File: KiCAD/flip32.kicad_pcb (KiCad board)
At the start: 2 copper layers, 36 x 36 mm, 57 parts, among them CON1 USB, IC2 MIC5205, Q1 MMBT29, U1 LP38691, U2 MPU-9150, U3 STM32F103CB, U5 MS5611-01BA, U6 CP2102, X1 8MHZ

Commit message: fixed some missing labels
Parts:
- added G***: LOGO, temp:bear-paw-med, B.Cu at (144.1, 151.3)
- renumbered JP2 to FSYNC-MPU
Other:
- board text added: "Twist32+"
- board text added: "by S.Antonio"
- board text added: "by S.Antonio 2015"
- board text added: "https://github.com/simonantonio/flip32plus/tree/mpu9150"
- board text added: "rev 20150717"

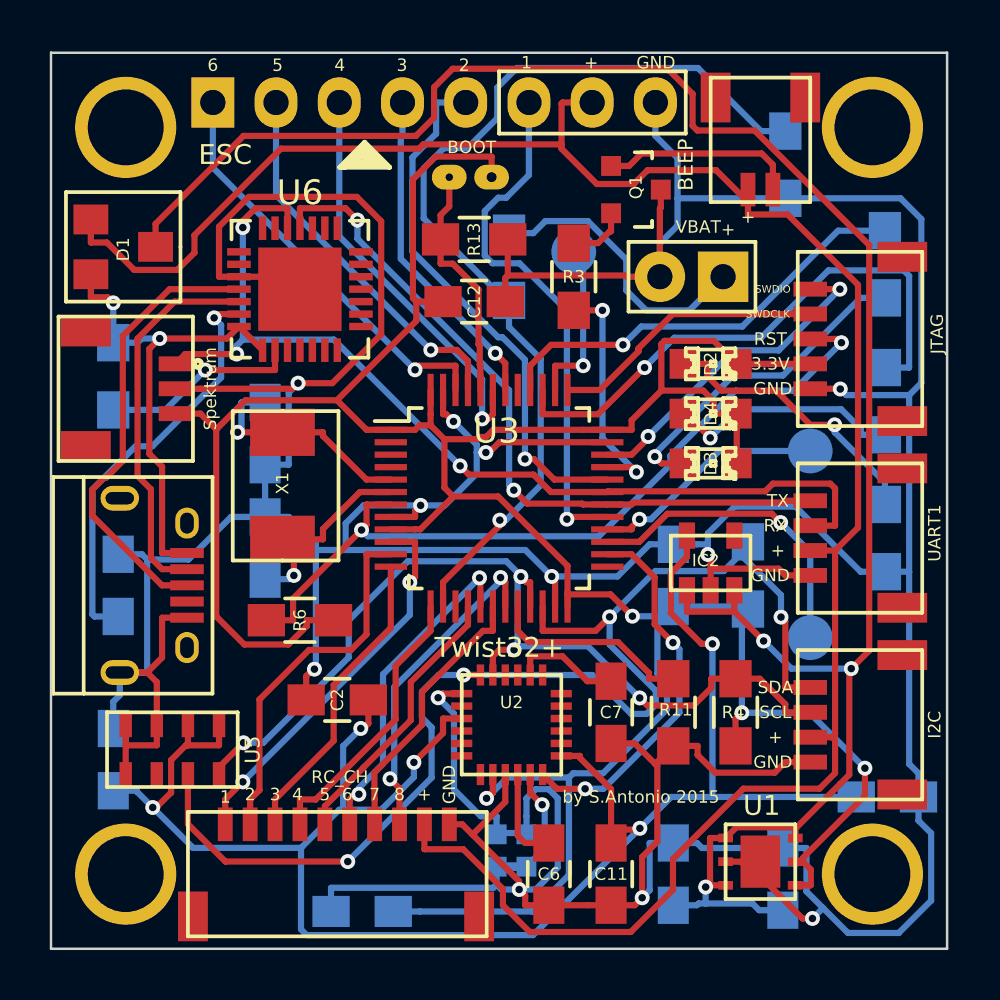
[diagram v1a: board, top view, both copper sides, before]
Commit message: swapped from old mpu9150 to newer mpu9250
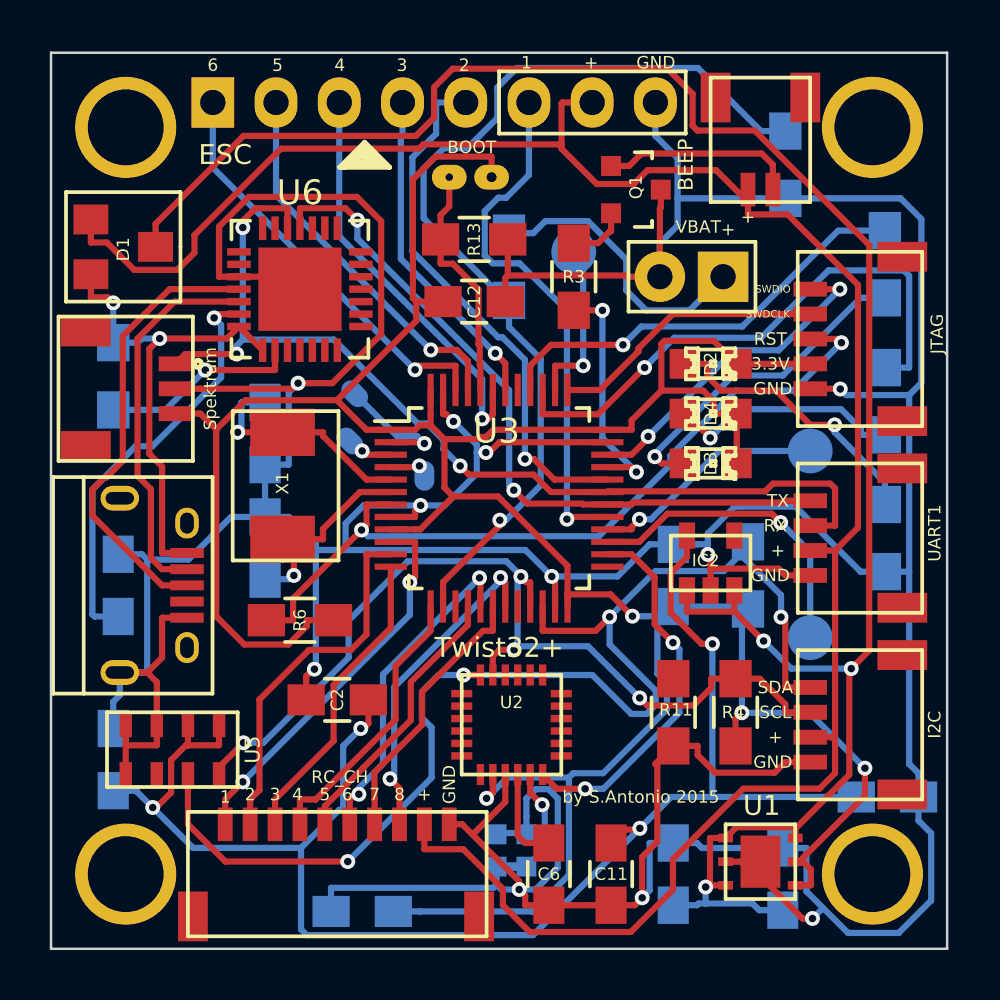
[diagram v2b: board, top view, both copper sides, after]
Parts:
- removed C7: 2.2nF 50v, Capacitors_SMD:C_0805_HandSoldering
- added PC13: UU5, Connect:1pin, B.Cu at (140.2, 141.7)
- added PC14: UU5, Connect:1pin, B.Cu at (140.0, 143.6)
- added PC15: UU5, Connect:1pin, B.Cu at (143.0, 145.0)
- U2: value MPU-9150 -> MPU-9250
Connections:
- U2 pad 1: N-0000024 -> (no net)
- U2 pad 18: N-0000071 -> GND
- U2 pad 20: N-0000032 -> GND
- U2 pad 22: N-0000052 -> VCC
- U2 pad 3: /VCC_SEN -> (no net)
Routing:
- net /VCC_SEN: track 74.5 -> 63.3 mm, vias 5 -> 4
- net /BOOT1: track 8.16 -> 0.00 mm
- net N-0000024: track 7.85 -> 0.00 mm, vias 1 -> 0
- net /UU3: track 0.00 -> 5.00 mm, vias 0 -> 1
- net N-0000032: track 4.41 -> 0.00 mm
- net GND: track 248.8 -> 246.7 mm
- net /UU4: track 0.00 -> 1.88 mm, vias 0 -> 1
- net /UU5: track 0.00 -> 1.65 mm, vias 0 -> 1

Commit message: redoing layout of traces for updated pinout of mpu9250
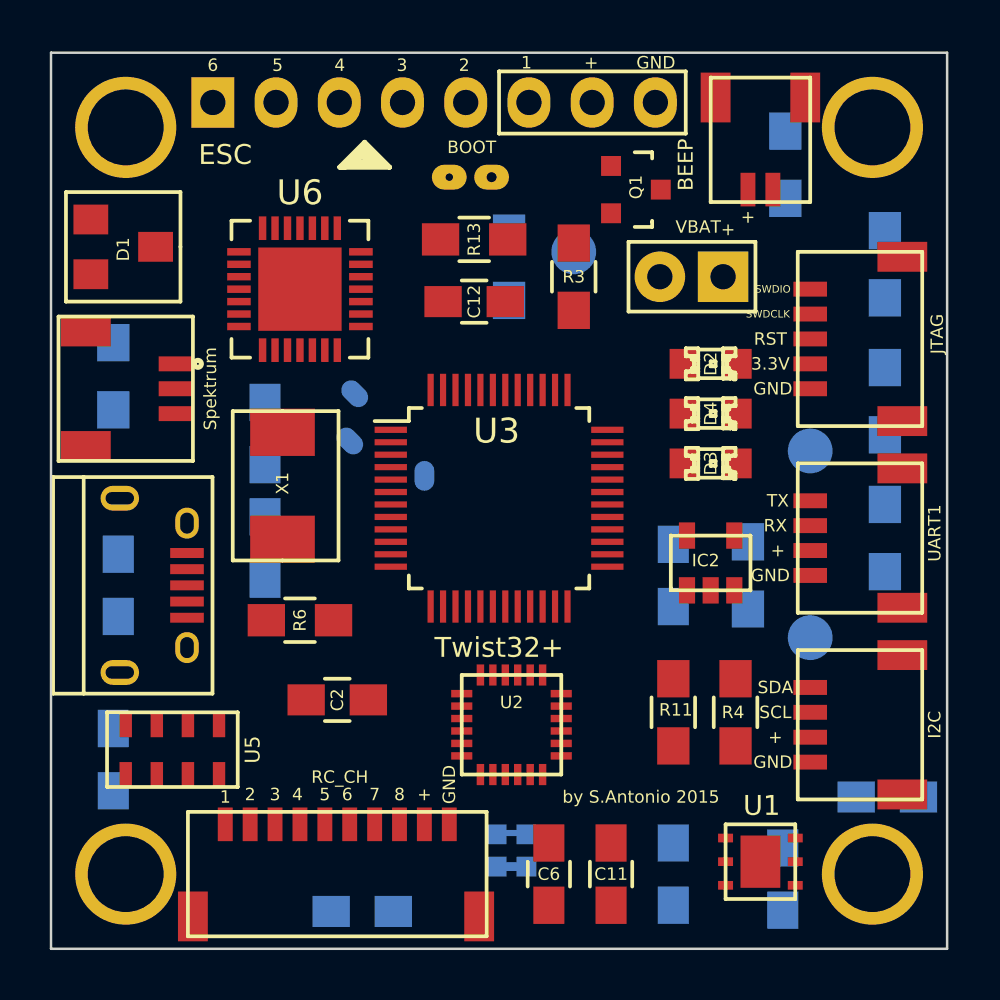
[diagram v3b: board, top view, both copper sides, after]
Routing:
- net GND: track 246.7 -> 0.00 mm, vias 11 -> 0
- net VCC: track 130.7 -> 0.00 mm, vias 4 -> 0
- net /VCC_IN: track 85.9 -> 0.00 mm
- net /TO_REGS: track 82.4 -> 0.00 mm, vias 3 -> 0
- net /VCC_SEN: track 63.3 -> 0.00 mm, vias 4 -> 0
- net /SDA: track 50.8 -> 0.00 mm, vias 4 -> 0
- net /RX0: track 40.1 -> 0.00 mm, vias 3 -> 0
- net /POWER_ADC: track 39.4 -> 0.00 mm, vias 1 -> 0
- net /SCL: track 37.4 -> 0.00 mm, vias 4 -> 0
- net /NRST: track 32.1 -> 0.00 mm, vias 2 -> 0
- net /TX0: track 29.0 -> 0.00 mm, vias 2 -> 0
- net /LED1: track 22.8 -> 0.00 mm, vias 1 -> 0
- net /PWM2: track 21.5 -> 0.00 mm, vias 1 -> 0
- net /PWM1: track 21.3 -> 0.00 mm, vias 1 -> 0
- net /VBUS: track 20.2 -> 0.00 mm, vias 2 -> 0
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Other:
- board text added: "https://github.com/simonantonio/flip32plus/tree/mpu9250"
- board text added: "rev 20150720"
- board text removed: "https://github.com/simonantonio/flip32plus/tree/mpu9150"
- board text removed: "rev 20150717"

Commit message: pcb completed
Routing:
- net GND: track 0.00 -> 250.2 mm, vias 0 -> 5
- net VCC: track 0.00 -> 163.9 mm, vias 0 -> 7
- net /VCC_IN: track 0.00 -> 124.0 mm, vias 0 -> 3
- net /VCC_SEN: track 0.00 -> 78.0 mm, vias 0 -> 3
- net /TO_REGS: track 0.00 -> 72.5 mm, vias 0 -> 4
- net /SDA: track 0.00 -> 57.7 mm, vias 0 -> 4
- net /TX0: track 0.00 -> 48.0 mm, vias 0 -> 4
- net /RX0: track 0.00 -> 46.0 mm, vias 0 -> 5
- net /NRST: track 0.00 -> 38.6 mm, vias 0 -> 2
- net /SCL: track 0.00 -> 36.3 mm, vias 0 -> 3
- net /LED0: track 0.00 -> 35.2 mm, vias 0 -> 1
- net /PWM2: track 0.00 -> 32.0 mm, vias 0 -> 2
- net /POWER_ADC: track 0.00 -> 31.9 mm, vias 0 -> 1
- net /PWM1: track 0.00 -> 31.6 mm, vias 0 -> 1
- net /UU8: track 0.00 -> 30.2 mm, vias 0 -> 1
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
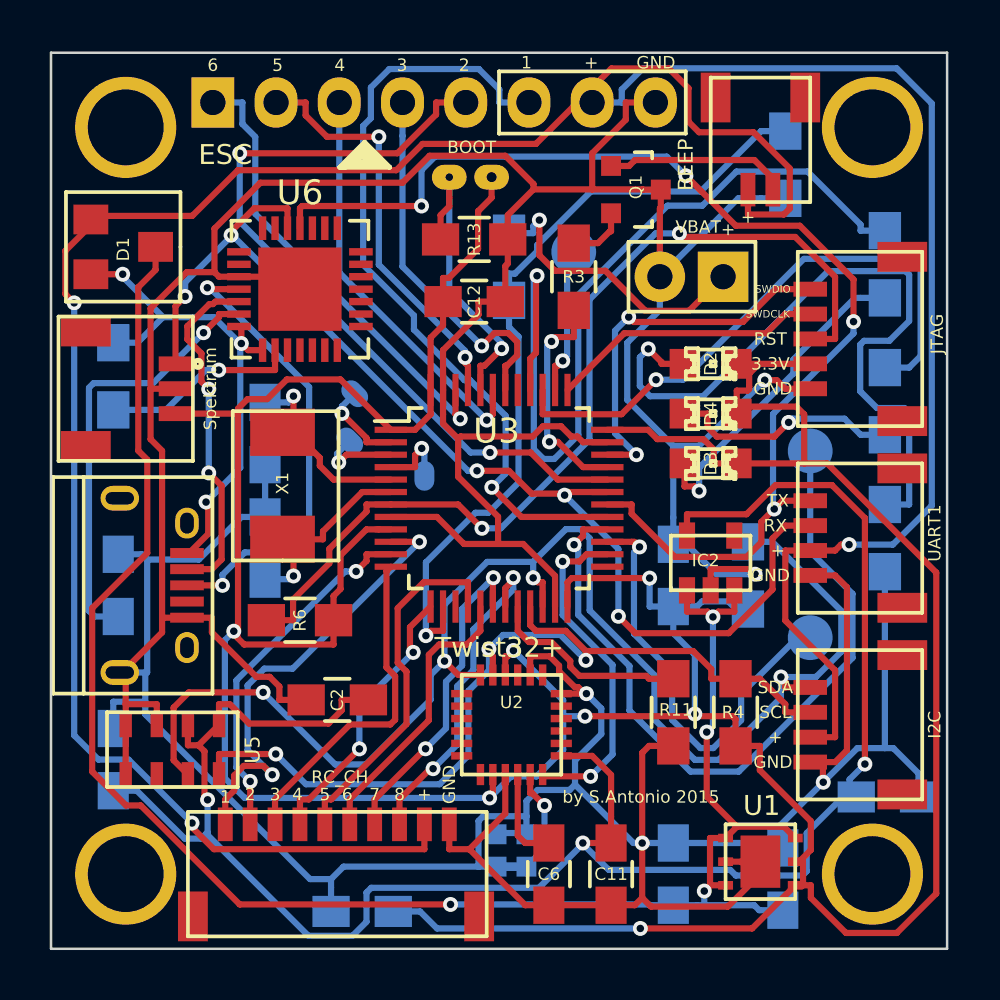
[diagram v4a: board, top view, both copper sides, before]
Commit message: optimize layout, reduced track length, reduced via count
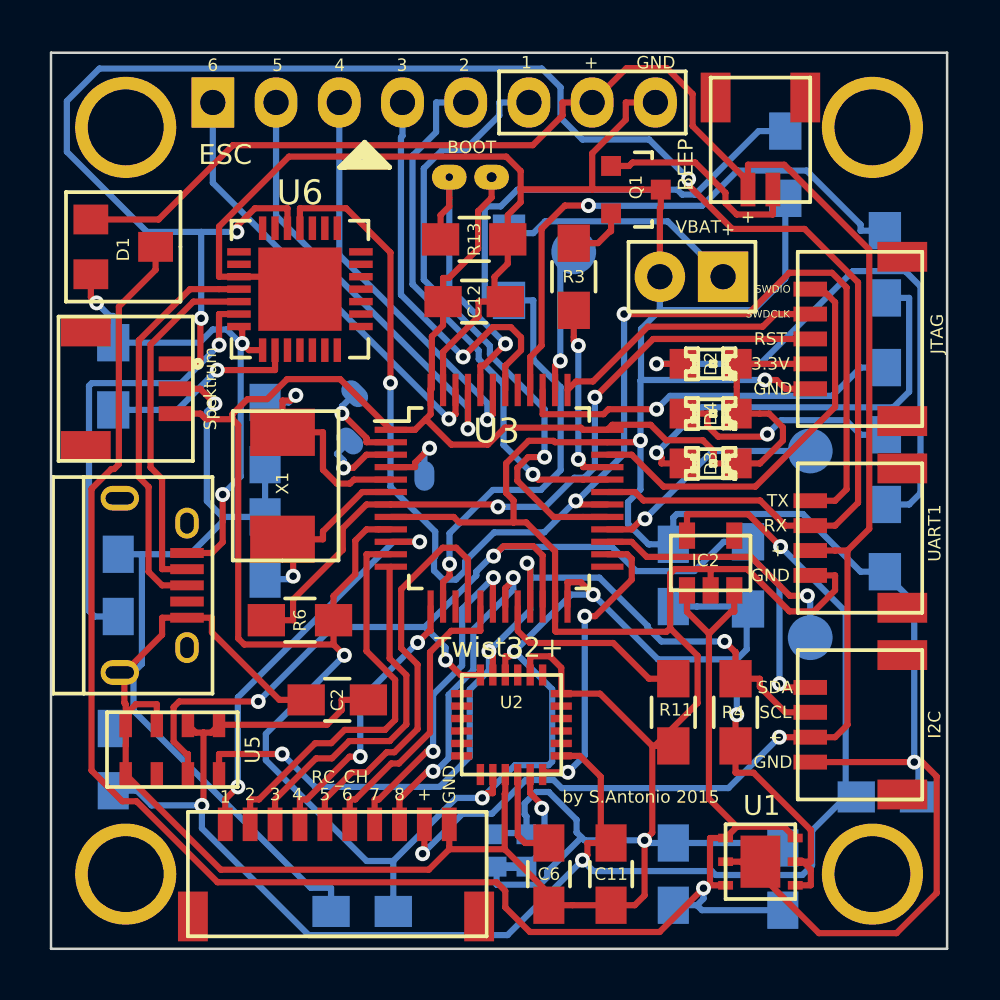
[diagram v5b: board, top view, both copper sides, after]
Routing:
- net /VCC_IN: track 124.0 -> 80.7 mm, vias 3 -> 2
- net VCC: track 163.9 -> 127.0 mm, vias 7 -> 5
- net /RX0: track 46.0 -> 76.5 mm, vias 5 -> 3
- net /UU8: track 30.2 -> 9.45 mm
- net GND: track 250.2 -> 268.8 mm
- net /LED0: track 35.2 -> 22.6 mm
- net /SDA: track 57.7 -> 45.1 mm
- net /PWM2: track 32.0 -> 21.6 mm, vias 2 -> 1
- net /NRST: track 38.6 -> 29.2 mm
- net /LED1: track 24.0 -> 15.5 mm
- net /VCC_SEN: track 78.0 -> 70.1 mm
- net /TX0: track 48.0 -> 55.4 mm, vias 4 -> 3
- net /UU7: track 17.5 -> 10.7 mm
- net /PWM1: track 31.6 -> 25.2 mm
- net N-0000076: track 29.6 -> 23.4 mm
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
